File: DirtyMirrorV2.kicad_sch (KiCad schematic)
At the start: 72 parts, among them J1 PWR, J2 ScopeGroundLoop, SW1 SW_SPDT, U1 TL072, U2 TL074, U3 TL074

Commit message: component layout
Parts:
- removed J2: ScopeGroundLoop, Connector_Pin:THT_GND_WIRE, symbol Connector:ScopeGroundLoop
- added J2: (no value), Connector:BatteryContact_Keystone_243, symbol Connector:GroundingSpring
- added J3: Power, Connector_BarrelJack:BarrelJack_Horizontal, symbol Connector:Barrel_Jack_Switch
- added R35: 1M, Resistor_SMD:R_0805_2012Metric, symbol Device:R_US
- C2: value 100u -> 10u
- R10, R7: value 51k -> 56k
- R16, R18: value 39k -> 47k
- R5: value 33k -> 47k
- SW1: footprint Connector_PinSocket_2.54mm:PinSocket_1x03_P2.54mm_Vertical -> Button_Switch_THT:Toggle_Dailywell_SubMini_SPDT
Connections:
- net +9V: now also J3.2; no longer J1.3 (Pin_3)
- net 0: now also J2.1
- net Bias: now also R5.1, U3.3 (+), R35.2; no longer U1.3 (+), U3.12 (+)
- net FxFull: now also U3.13 (-), U3.14; no longer U3.1, U3.2 (-)
- net FxRaw: now also U3.1; no longer U3.14
- net at R30.2, R31.2, R33.1: now also U3.2 (-); no longer U3.13 (-)
- net at C3.2: now also U1.3 (+), R35.1; no longer R5.1
- net at C6.1, R19.2: now also U3.12 (+); no longer U3.3 (+)
- new net Low_In: J1.3 (Pin_3), J3.1
- no-connect marks 0 -> 1
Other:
- moved on the sheet: C11, C3, R3, RV1, U3A, U3D, U3E

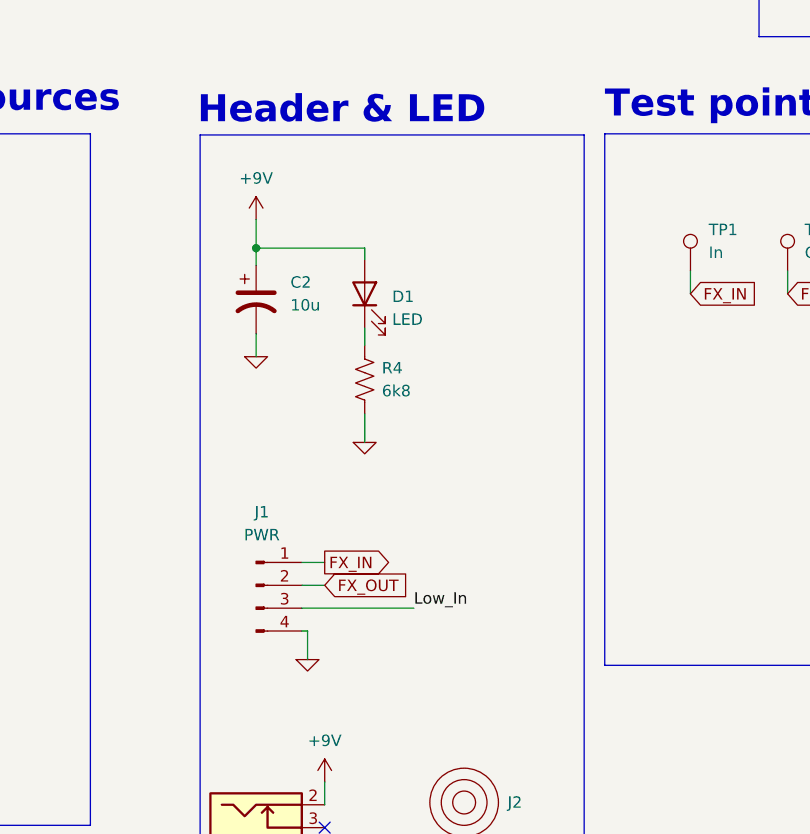
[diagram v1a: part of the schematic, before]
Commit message: moved bulk capacitor, silkscreen
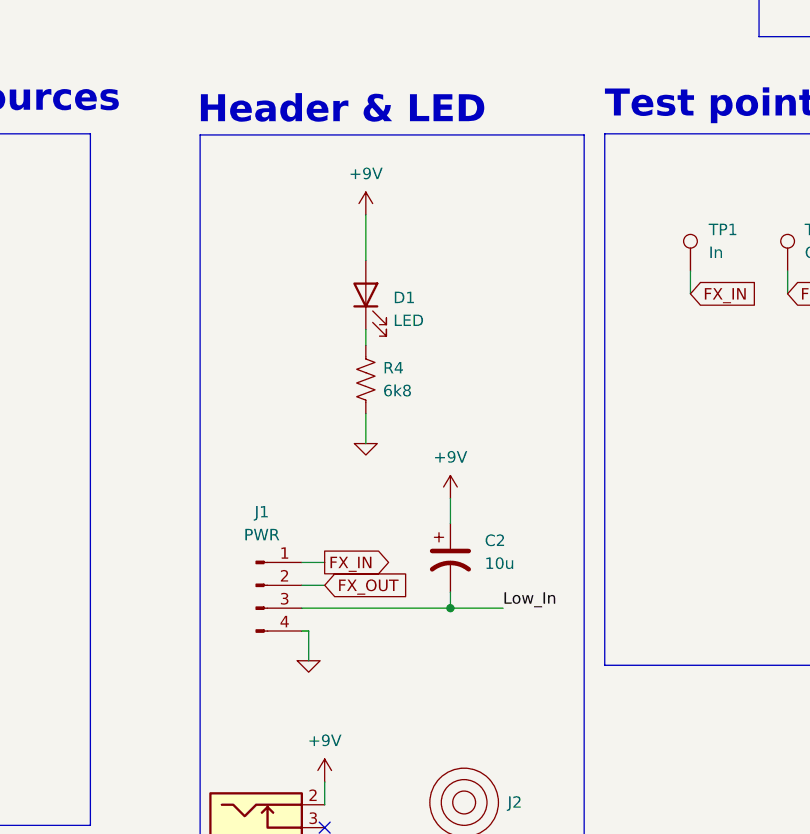
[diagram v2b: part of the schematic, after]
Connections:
- net 0: no longer C2.2
- net Low_In: now also C2.2
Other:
- moved on the sheet: C2

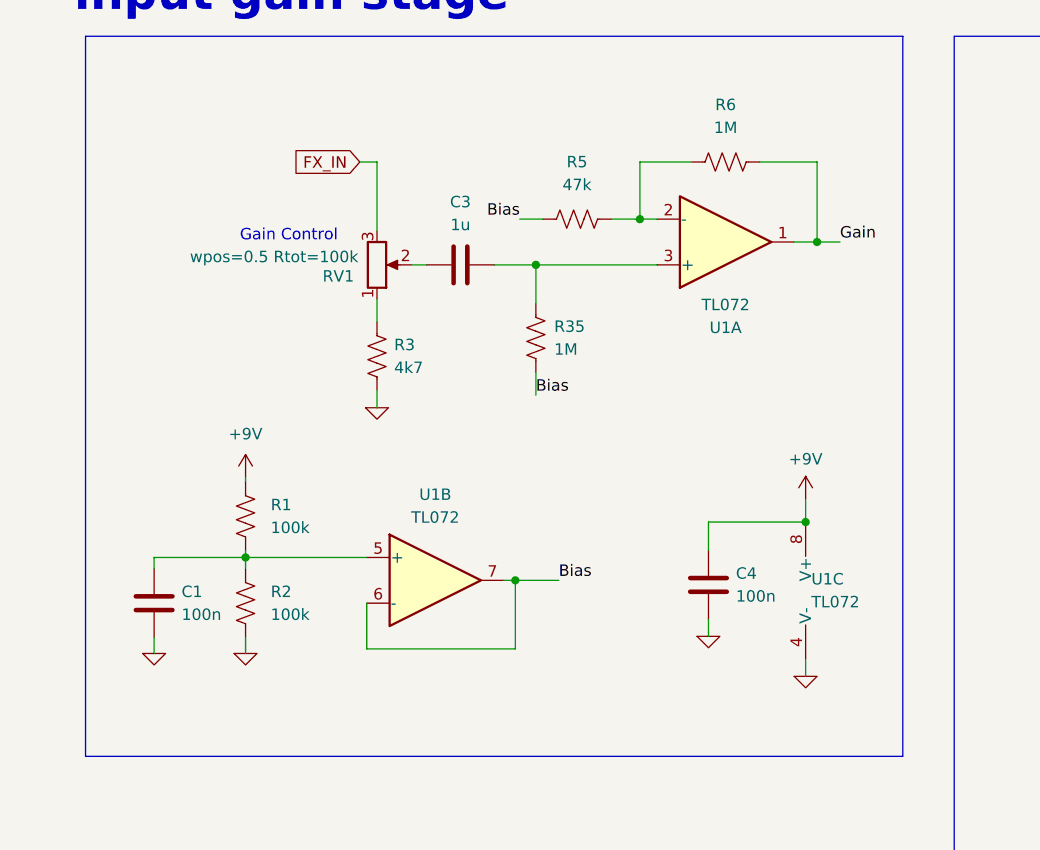
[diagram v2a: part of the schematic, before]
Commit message: switched u1 circuitry to always on
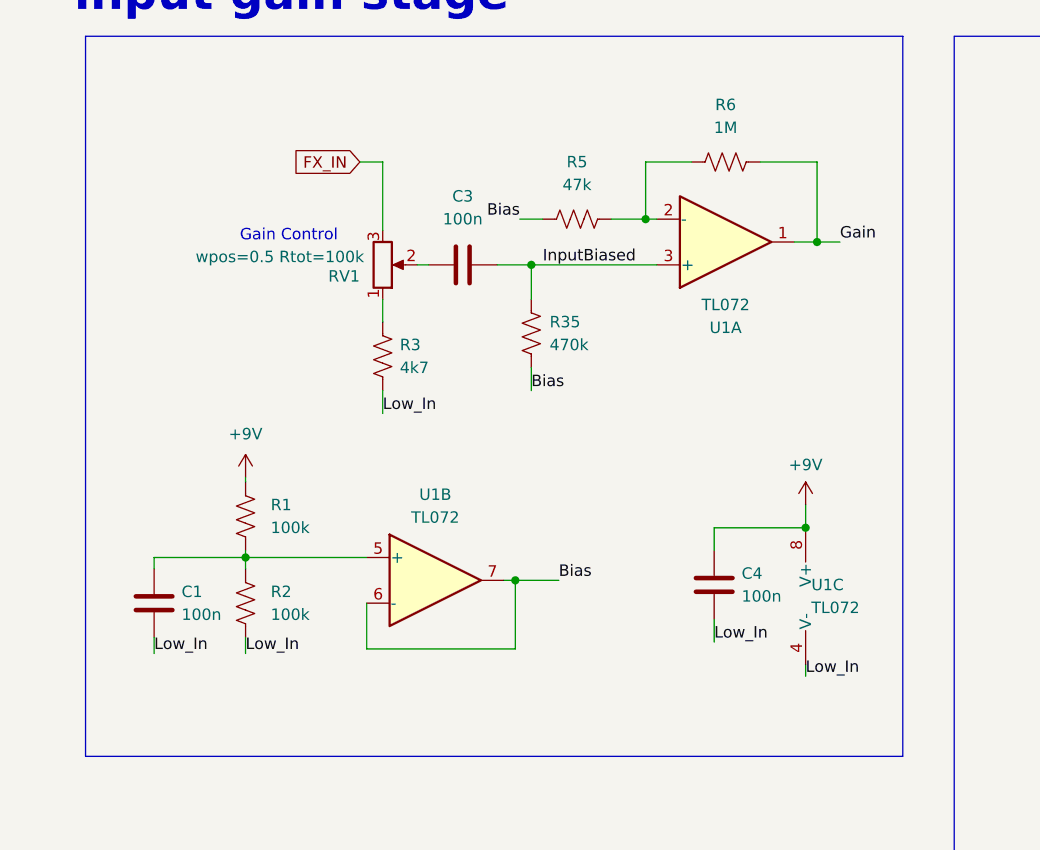
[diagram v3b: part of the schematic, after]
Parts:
- C3: value 1u -> 100n
- R35: value 1M -> 470k
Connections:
- net 0: no longer C1.2, C4.2, R2.2, R3.2, U1.4 (V-)
- net Low_In: now also C1.2, C4.2, R2.2, R3.2, U1.4 (V-)
- net InputBiased: now reaches C3.2, R35.1, U1.3 (+)
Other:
- moved on the sheet: C4, R3, R35, RV1, U1C

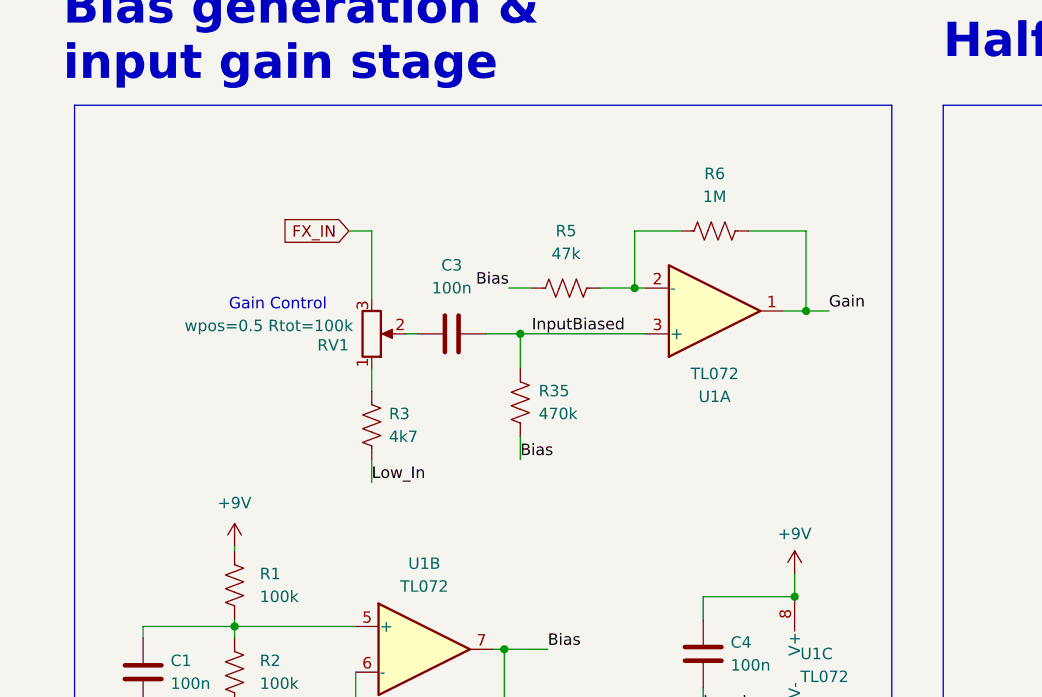
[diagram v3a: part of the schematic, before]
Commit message: moved gain control to feedback loop
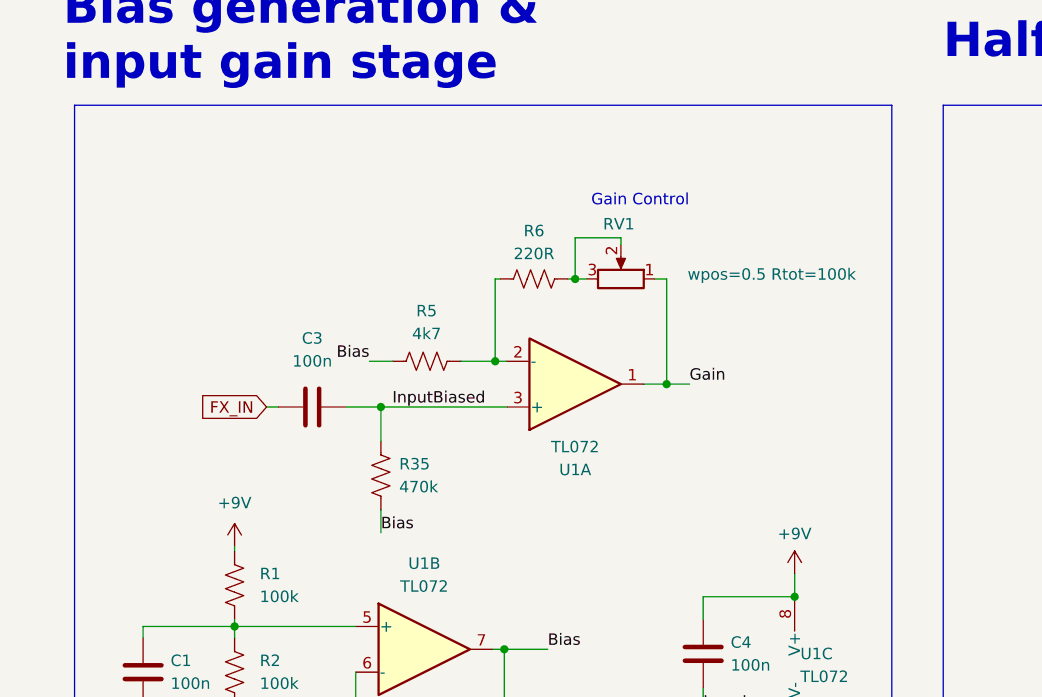
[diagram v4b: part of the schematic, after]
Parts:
- removed R3: 4k7, Resistor_SMD:R_0805_2012Metric, symbol Device:R_US
- R5: value 47k -> 4k7
- R6: value 1M -> 220R
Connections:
- net FX_IN: now also C3.1; no longer RV1.3
- net Gain: now also RV1.1; no longer R6.2
- net at RV1.2: now also R6.2, RV1.3; no longer C3.1
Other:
- moved on the sheet: C3, R35, R5, R6, RV1, U1A

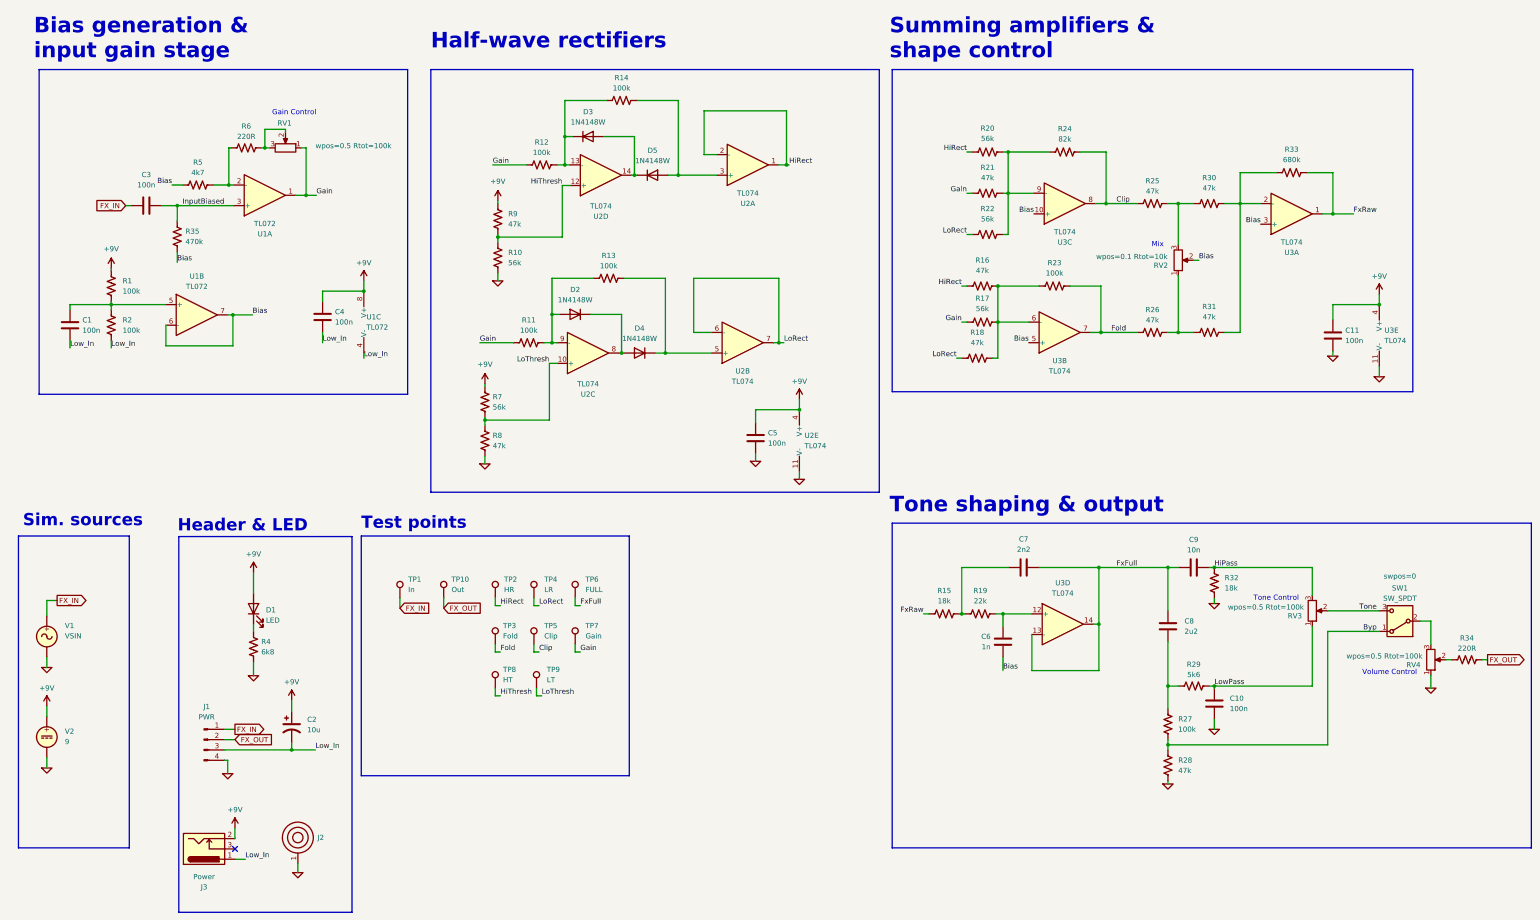
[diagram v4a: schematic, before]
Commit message: grounding tweaks and corner bevels
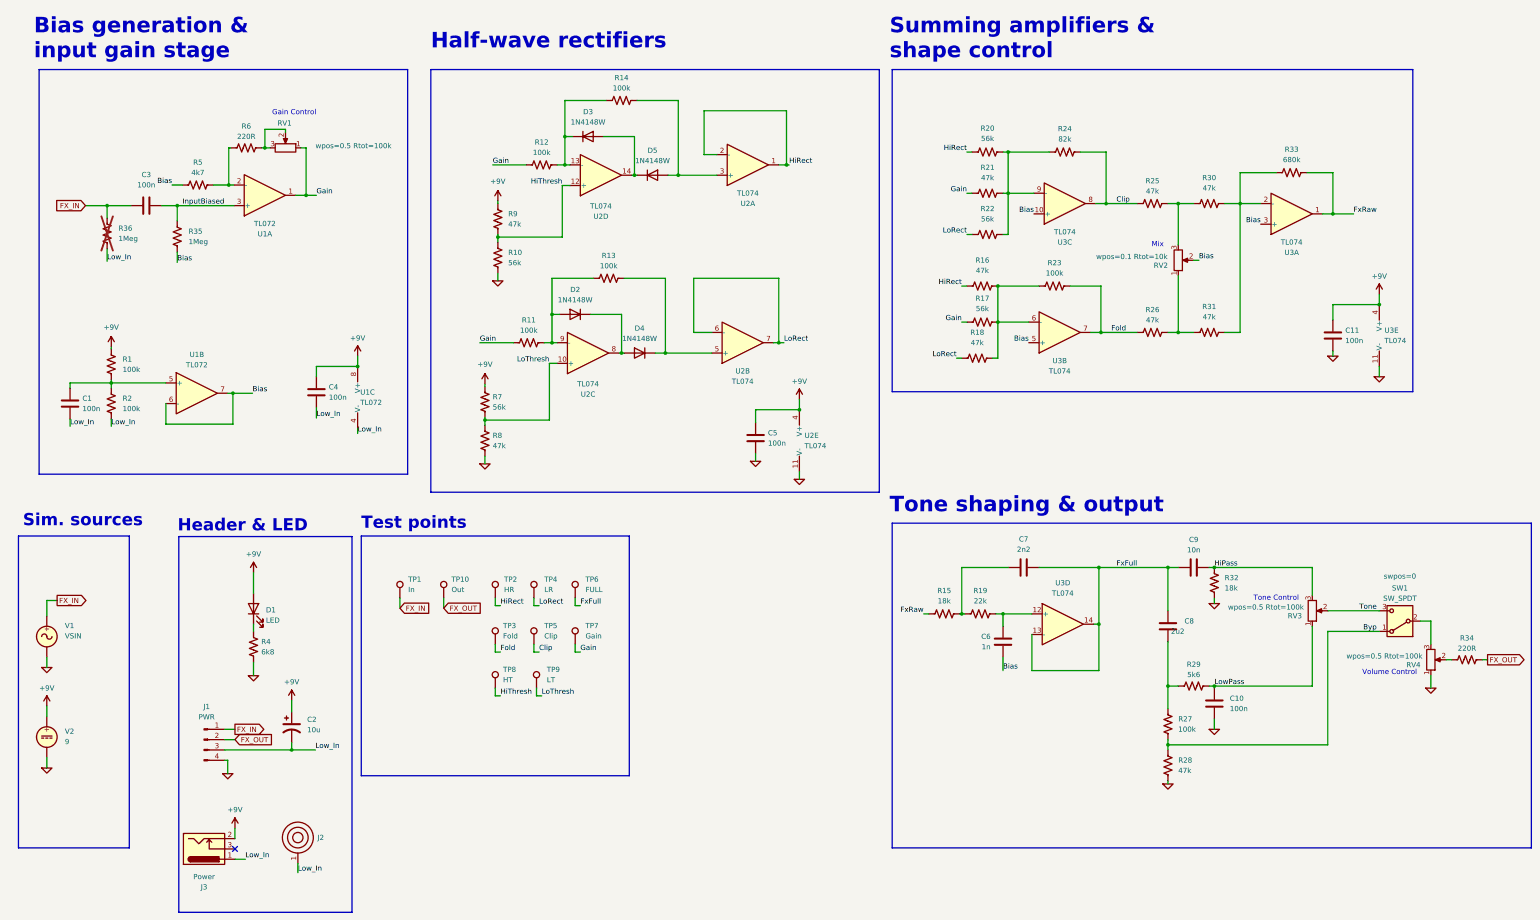
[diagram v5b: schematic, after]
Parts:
- added R36: 1Meg, Resistor_SMD:R_0805_2012Metric, symbol Device:R_US
- R35: value 470k -> 1Meg
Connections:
- net 0: no longer J2.1
- net FX_IN: now also R36.1
- net Low_In: now also J2.1, R36.2
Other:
- moved on the sheet: C1, C4, R1, R2, U1B, U1C
